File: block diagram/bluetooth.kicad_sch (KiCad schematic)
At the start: 0 parts

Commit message: add actual content
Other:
- removed sheet filtering
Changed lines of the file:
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@@
 	(wire
 		(pts
-			(xy 165.1 74.93) (xy 180.34 74.93)
+			(xy 165.1 74.93) (xy 205.74 74.93)
 		)
 		(stroke
@@
 		(pts
 			(xy 205.74 104.14) (xy 261.62 104.14)
-		)
-		(stroke
-			(width 0)
-			(type default)
-		)
-	)
-	(wire
-		(pts
-			(xy 195.58 74.93) (xy 205.74 74.93)
 		)
 		(stroke
@@
 				)
 			)
-		)
-	)
-	(sheet
-		(at 180.34 60.96)
-		(size 15.24 26.67)
-		(exclude_from_sim no)
-		(in_bom yes)
-		(on_board yes)
-		(dnp no)
-		(fields_autoplaced yes)
-		(stroke
-			(width 0.1524)
-			(type solid)
-			(color 132 0 0 1)
-		)
-		(fill
-			(color 255 255 194 1.0000)
-		)
-		(property "Sheetname" "filtering"
-			(at 180.34 60.2484 0)
-			(effects
-				(font
-					(size 1.27 1.27)
-				)
-				(justify left bottom)
-			)
-		)
-		(property "Sheetfile" "untitled.kicad_sch"
-			(at 180.34 88.2146 0)
-			(effects
-				(font
-					(size 1.27 1.27)
-				)
-				(justify left top)
-			)
-		)
-		(instances
-			(project "block diagram"
-				(path "/77b537aa-abd1-4b45-8666-f13206102f09/06c90ba9-5280-426d-b704-62779bf0bf86"
-					(page "11")
-				)
-			)

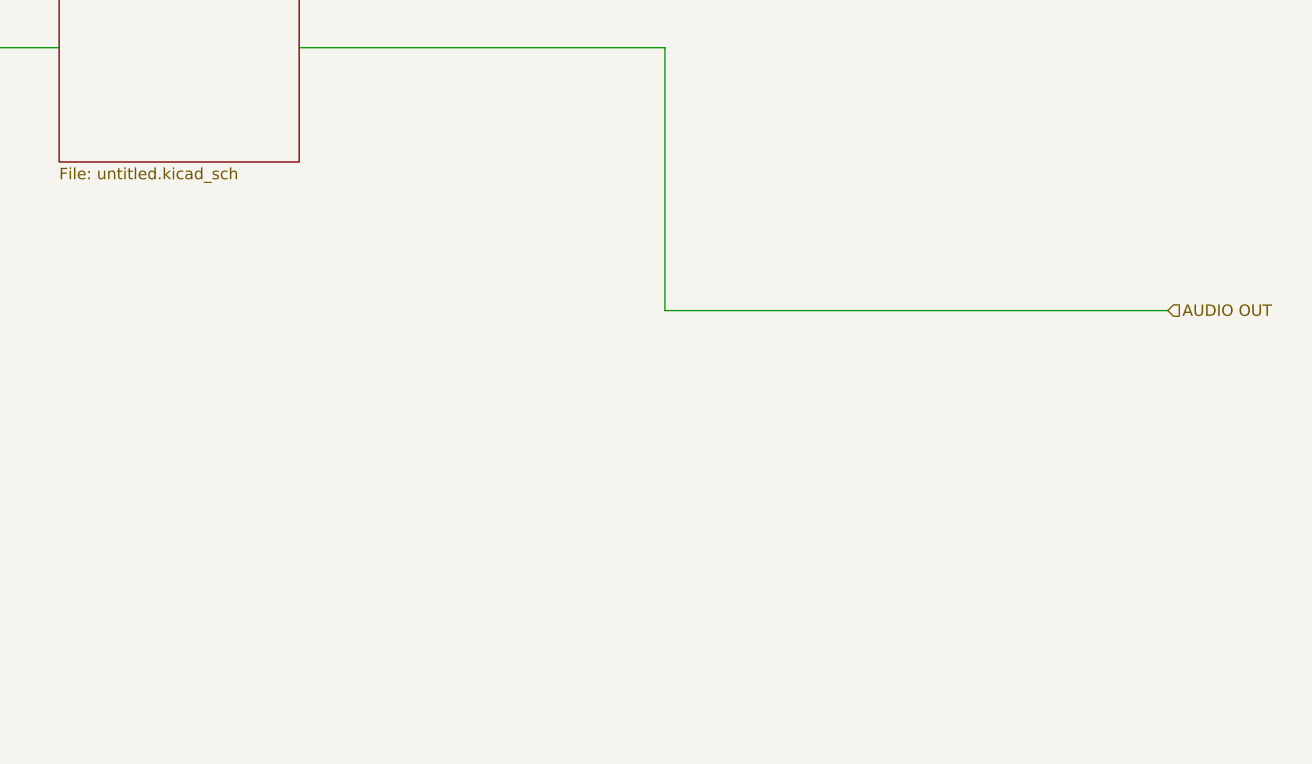
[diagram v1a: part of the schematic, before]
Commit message: battery spec added
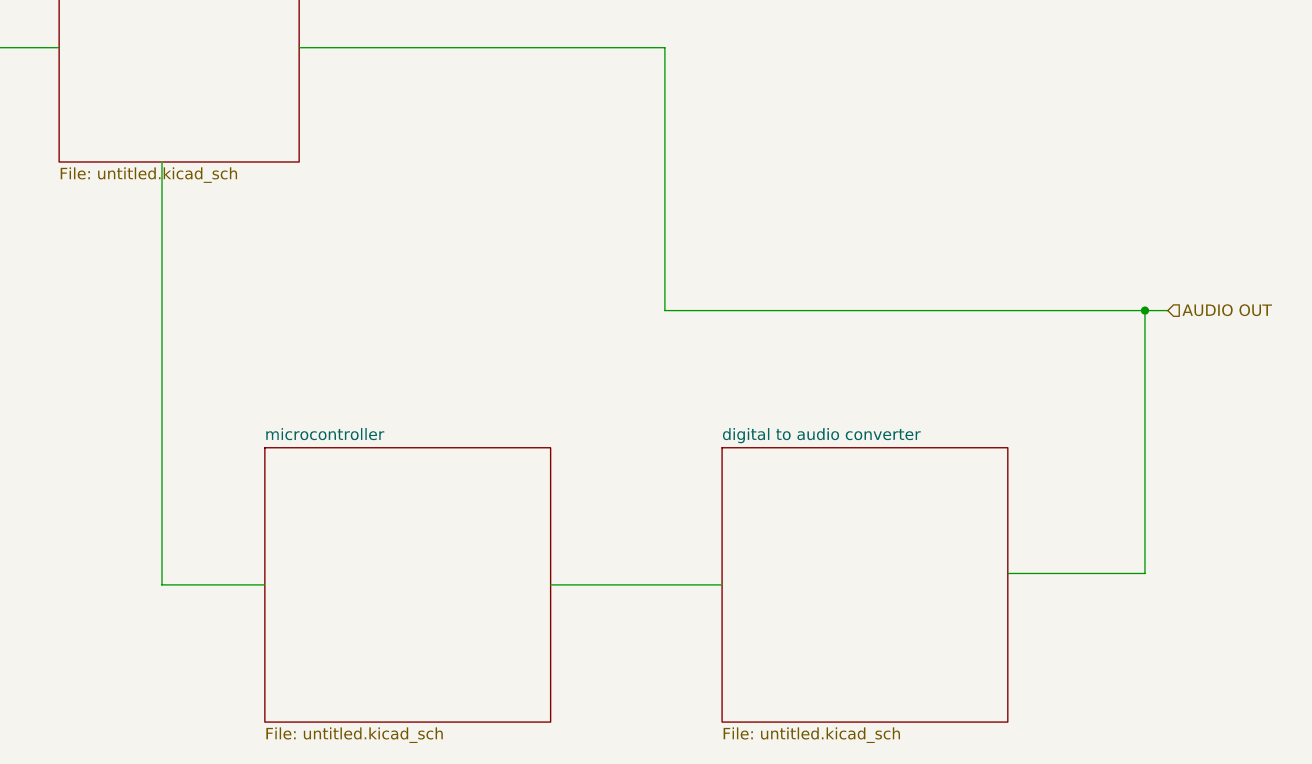
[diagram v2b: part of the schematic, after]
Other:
- added sheet digital to audio converter (untitled.kicad_sch)
- added sheet microcontroller (untitled.kicad_sch)
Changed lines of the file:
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@@
 	(generator_version "9.0")
 	(paper "A4")
+	(junction
+		(at 259.08 104.14)
+		(diameter 0)
+		(color 0 0 0 0)
+	)
 	(wire
 		(pts
@@
 	(wire
 		(pts
+			(xy 243.84 133.35) (xy 259.08 133.35)
+		)
+		(stroke
+			(width 0)
+			(type default)
+		)
+	)
+	(wire
+		(pts
 			(xy 116.84 35.56) (xy 116.84 62.23)
 		)
@@
 	(wire
 		(pts
+			(xy 149.86 87.63) (xy 149.86 134.62)
+		)
+		(stroke
+			(width 0)
+			(type default)
+		)
+	)
+	(wire
+		(pts
+			(xy 193.04 134.62) (xy 212.09 134.62)
+		)
+		(stroke
+			(width 0)
+			(type default)
+		)
+	)
+	(wire
+		(pts
 			(xy 139.7 31.75) (xy 53.34 31.75)
 		)
@@
 	(wire
 		(pts
-			(xy 205.74 104.14) (xy 261.62 104.14)
+			(xy 259.08 133.35) (xy 259.08 104.14)
+		)
+		(stroke
+			(width 0)
+			(type default)
+		)
+	)
+	(wire
+		(pts
+			(xy 205.74 104.14) (xy 259.08 104.14)
 		)
 		(stroke
@@
 	(wire
 		(pts
+			(xy 149.86 134.62) (xy 161.29 134.62)
+		)
+		(stroke
+			(width 0)
+			(type default)
+		)
+	)
+	(wire
+		(pts
 			(xy 60.96 74.93) (xy 71.12 74.93)
+		)
+		(stroke
+			(width 0)
+			(type default)
+		)
+	)
+	(wire
+		(pts
+			(xy 259.08 104.14) (xy 261.62 104.14)
 		)
 		(stroke
@@
 				)
 			)
+		)
+	)
+	(sheet
+		(at 161.29 119.38)
+		(size 31.75 30.48)
+		(exclude_from_sim no)
+		(in_bom yes)
+		(on_board yes)
+		(dnp no)
+		(fields_autoplaced yes)
+		(stroke
+			(width 0.1524)
+			(type solid)
+			(color 132 0 0 1)
+		)
+		(fill
+			(color 255 255 194 1.0000)
+		)
+		(property "Sheetname" "microcontroller"
+			(at 161.29 118.6684 0)
+			(effects
+				(font
+					(size 1.27 1.27)
+				)
+				(justify left bottom)
+			)
+		)
+		(property "Sheetfile" "untitled.kicad_sch"
+			(at 161.29 150.4446 0)
+			(effects
+				(font
+					(size 1.27 1.27)
+				)
+				(justify left top)
+			)
+		)
+		(instances
+			(project "block diagram"
+				(path "/77b537aa-abd1-4b45-8666-f13206102f09/06c90ba9-5280-426d-b704-62779bf0bf86"
+					(page "11")
+				)
+			)
+		)
+	)
+	(sheet
+		(at 212.09 119.38)
+		(size 31.75 30.48)
+		(exclude_from_sim no)
+		(in_bom yes)
+		(on_board yes)
+		(dnp no)
+		(fields_autoplaced yes)
+		(stroke
+			(width 0.1524)
+			(type solid)
+			(color 132 0 0 1)
+		)
+		(fill
+			(color 255 255 194 1.0000)
+		)
+		(property "Sheetname" "digital to audio converter"
+			(at 212.09 118.6684 0)
+			(effects
+				(font
+					(size 1.27 1.27)
+				)
+				(justify left bottom)
+			)
+		)
+		(property "Sheetfile" "untitled.kicad_sch"
+			(at 212.09 150.4446 0)
+			(effects
+				(font
+					(size 1.27 1.27)
+				)
+				(justify left top)
+			)
+		)
+		(instances
+			(project "block diagram"
+				(path "/77b537aa-abd1-4b45-8666-f13206102f09/06c90ba9-5280-426d-b704-62779bf0bf86"
+					(page "12")
+				)
+			)

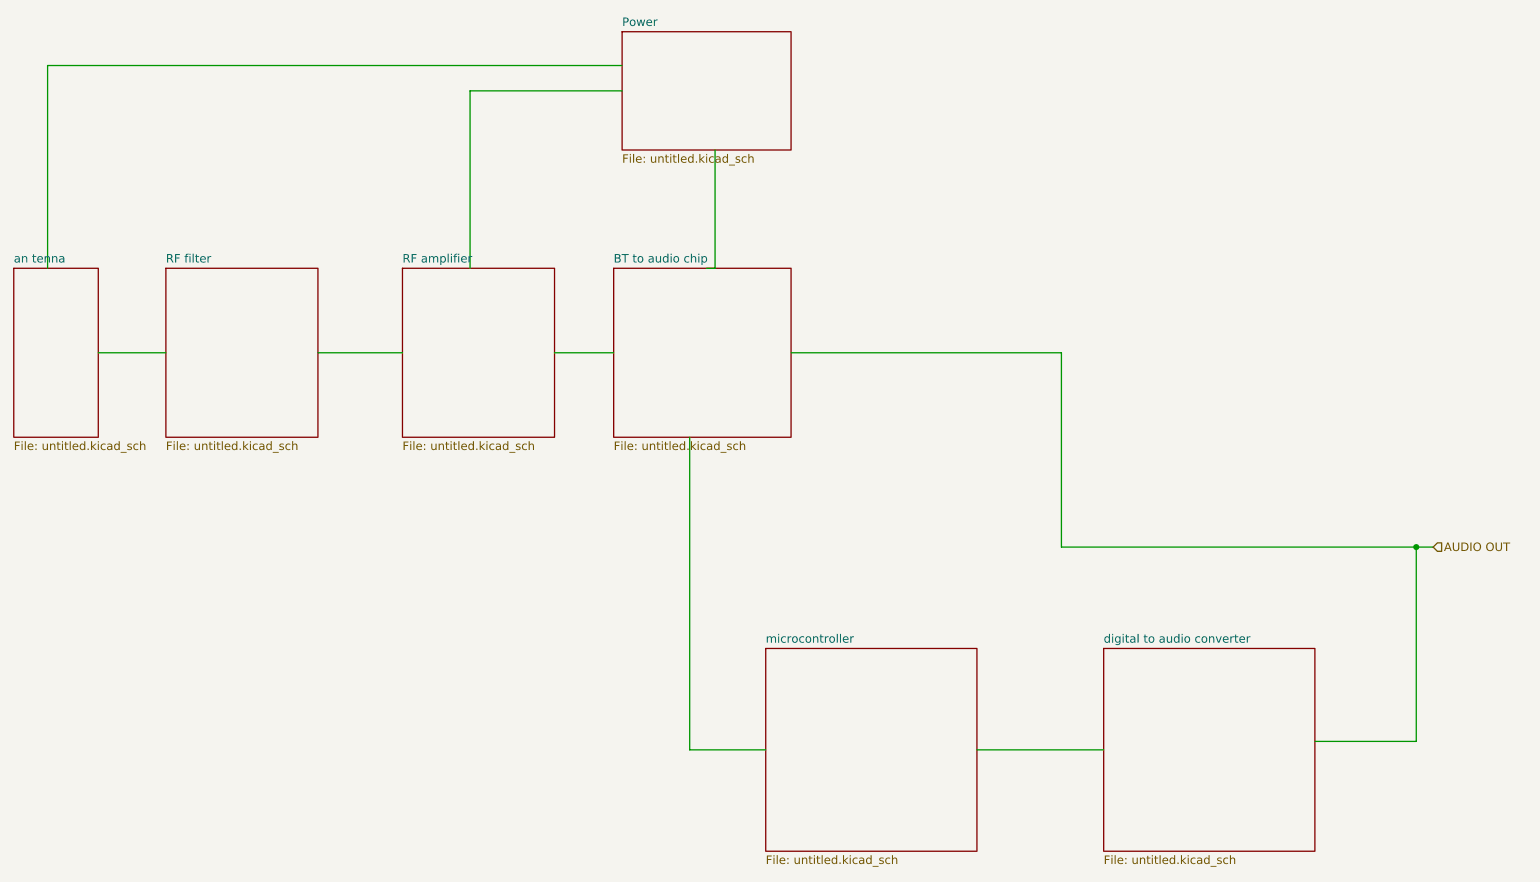
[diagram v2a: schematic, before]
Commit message: diagrammed bt chip, please fix formatting
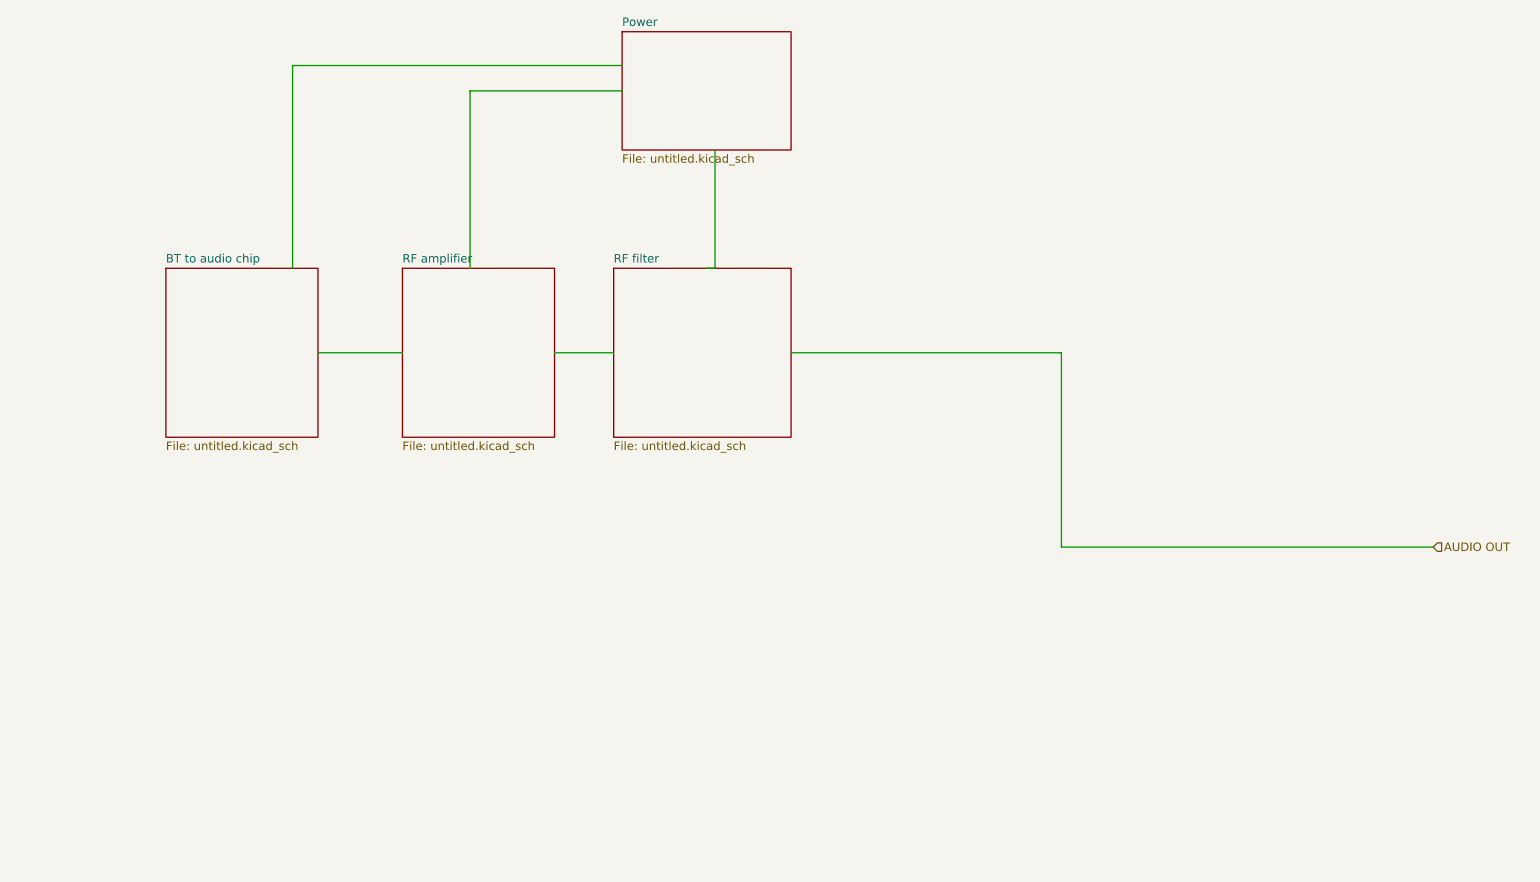
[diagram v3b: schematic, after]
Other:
- removed sheet an tenna
- removed sheet digital to audio converter
- removed sheet microcontroller
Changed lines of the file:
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@@
 (kicad_sch
-	(version 20250114)
+	(version 20260306)
 	(generator "eeschema")
-	(generator_version "9.0")
+	(generator_version "10.0")
 	(paper "A4")
-	(junction
-		(at 259.08 104.14)
-		(diameter 0)
-		(color 0 0 0 0)
-	)
-	(wire
-		(pts
-			(xy 53.34 31.75) (xy 53.34 62.23)
+	(wire
+		(pts
+			(xy 90.17 31.75) (xy 90.17 62.23)
 		)
 		(stroke
@@
 	(wire
 		(pts
-			(xy 243.84 133.35) (xy 259.08 133.35)
-		)
-		(stroke
-			(width 0)
-			(type default)
-		)
-	)
-	(wire
-		(pts
 			(xy 116.84 35.56) (xy 116.84 62.23)
 		)
@@
 	(wire
 		(pts
-			(xy 149.86 87.63) (xy 149.86 134.62)
-		)
-		(stroke
-			(width 0)
-			(type default)
-		)
-	)
-	(wire
-		(pts
-			(xy 193.04 134.62) (xy 212.09 134.62)
-		)
-		(stroke
-			(width 0)
-			(type default)
-		)
-	)
-	(wire
-		(pts
-			(xy 139.7 31.75) (xy 53.34 31.75)
-		)
-		(stroke
-			(width 0)
-			(type default)
-		)
-	)
-	(wire
-		(pts
 			(xy 205.74 74.93) (xy 205.74 104.14)
 		)
@@
 	(wire
 		(pts
-			(xy 259.08 133.35) (xy 259.08 104.14)
-		)
-		(stroke
-			(width 0)
-			(type default)
-		)
-	)
-	(wire
-		(pts
-			(xy 205.74 104.14) (xy 259.08 104.14)
+			(xy 205.74 104.14) (xy 261.62 104.14)
+		)
+		(stroke
+			(width 0)
+			(type default)
+		)
+	)
+	(wire
+		(pts
+			(xy 139.7 31.75) (xy 90.17 31.75)
 		)
 		(stroke
@@
 		(pts
 			(xy 93.98 74.93) (xy 106.68 74.93)
-		)
-		(stroke
-			(width 0)
-			(type default)
-		)
-	)
-	(wire
-		(pts
-			(xy 149.86 134.62) (xy 161.29 134.62)
-		)
-		(stroke
-			(width 0)
-			(type default)
-		)
-	)
-	(wire
-		(pts
-			(xy 60.96 74.93) (xy 71.12 74.93)
-		)
-		(stroke
-			(width 0)
-			(type default)
-		)
-	)
-	(wire
-		(pts
-			(xy 259.08 104.14) (xy 261.62 104.14)
 		)
 		(stroke
@@
 		)
 		(fill
-			(color 255 255 194 1.0000)
+			(color 255 255 194 1)
 		)
 		(property "Sheetname" "RF amplifier"
 			(at 106.68 61.5184 0)
+			(show_name no)
+			(do_not_autoplace no)
 			(effects
 				(font
@@
 		(property "Sheetfile" "untitled.kicad_sch"
 			(at 106.68 88.2146 0)
+			(show_name no)
+			(do_not_autoplace no)
 			(effects
 				(font
@@
 	)
 	(sheet
-		(at 161.29 119.38)
-		(size 31.75 30.48)
-		(exclude_from_sim no)
-		(in_bom yes)
-		(on_board yes)
-		(dnp no)
-		(fields_autoplaced yes)
-		(stroke
-			(width 0.1524)
-			(type solid)
-			(color 132 0 0 1)
-		)
-		(fill
-			(color 255 255 194 1.0000)
-		)
-		(property "Sheetname" "microcontroller"
-			(at 161.29 118.6684 0)
-			(effects
-				(font
-					(size 1.27 1.27)
-				)
-				(justify left bottom)
-			)
-		)
-		(property "Sheetfile" "untitled.kicad_sch"
-			(at 161.29 150.4446 0)
-			(effects
-				(font
-					(size 1.27 1.27)
-				)
-				(justify left top)
-			)
-		)
-		(instances
-			(project "block diagram"
-				(path "/77b537aa-abd1-4b45-8666-f13206102f09/06c90ba9-5280-426d-b704-62779bf0bf86"
-					(page "11")
-				)
-			)
-		)
-	)
-	(sheet
-		(at 212.09 119.38)
-		(size 31.75 30.48)
-		(exclude_from_sim no)
-		(in_bom yes)
-		(on_board yes)
-		(dnp no)
-		(fields_autoplaced yes)
-		(stroke
-			(width 0.1524)
-			(type solid)
-			(color 132 0 0 1)
-		)
-		(fill
-			(color 255 255 194 1.0000)
-		)
-		(property "Sheetname" "digital to audio converter"
-			(at 212.09 118.6684 0)
-			(effects
-				(font
-					(size 1.27 1.27)
-				)
-				(justify left bottom)
-			)
-		)
-		(property "Sheetfile" "untitled.kicad_sch"
-			(at 212.09 150.4446 0)
-			(effects
-				(font
-					(size 1.27 1.27)
-				)
-				(justify left top)
-			)
-		)
-		(instances
-			(project "block diagram"
-				(path "/77b537aa-abd1-4b45-8666-f13206102f09/06c90ba9-5280-426d-b704-62779bf0bf86"
-					(page "12")
-				)
-			)
-		)
-	)
-	(sheet
 		(at 139.7 26.67)
 		(size 25.4 17.78)
@@
 		)
 		(fill
-			(color 255 255 194 1.0000)
+			(color 255 255 194 1)
 		)
 		(property "Sheetname" "Power"
 			(at 139.7 25.9584 0)
+			(show_name no)
+			(do_not_autoplace no)
 			(effects
 				(font
@@
 		(property "Sheetfile" "untitled.kicad_sch"
 			(at 139.7 45.0346 0)
+			(show_name no)
+			(do_not_autoplace no)
 			(effects
 				(font
@@
 		(property "Field2" ""
 			(at 139.7 26.67 0)
+			(show_name no)
+			(do_not_autoplace no)
 			(effects
 				(font
@@
 		)
 		(fill
-			(color 255 255 194 1.0000)
-		)
-		(property "Sheetname" "BT to audio chip"
+			(color 255 255 194 1)
+		)
+		(property "Sheetname" "RF filter"
 			(at 138.43 61.5184 0)
+			(show_name no)
+			(do_not_autoplace no)
 			(effects
 				(font
@@
 		(property "Sheetfile" "untitled.kicad_sch"
 			(at 138.43 88.2146 0)
+			(show_name no)
+			(do_not_autoplace no)
 			(effects
 				(font
@@
 	)
 	(sheet
-		(at 48.26 62.23)
-		(size 12.7 25.4)
-		(exclude_from_sim no)
-		(in_bom yes)
-		(on_board yes)
-		(dnp no)
-		(fields_autoplaced yes)
-		(stroke
-			(width 0.1524)
-			(type solid)
-			(color 132 0 0 1)
-		)
-		(fill
-			(color 255 255 194 1.0000)
-		)
-		(property "Sheetname" "an tenna"
-			(at 48.26 61.5184 0)
-			(effects
-				(font
-					(size 1.27 1.27)
-				)
-				(justify left bottom)
-			)
-		)
-		(property "Sheetfile" "untitled.kicad_sch"
-			(at 48.26 88.2146 0)
-			(effects
-				(font
-					(size 1.27 1.27)
-				)
-				(justify left top)
-			)
-		)
-		(instances
-			(project "block diagram"
-				(path "/77b537aa-abd1-4b45-8666-f13206102f09/06c90ba9-5280-426d-b704-62779bf0bf86"
-					(page "7")
-				)
-			)
-		)
-	)
-	(sheet
 		(at 71.12 62.23)
 		(size 22.86 25.4)
@@
 		)
 		(fill
-			(color 255 255 194 1.0000)
-		)
-		(property "Sheetname" "RF filter"
+			(color 255 255 194 1)
+		)
+		(property "Sheetname" "BT to audio chip"
 			(at 71.12 61.5184 0)
+			(show_name no)
+			(do_not_autoplace no)
 			(effects
 				(font
@@
 		(property "Sheetfile" "untitled.kicad_sch"
 			(at 71.12 88.2146 0)
-			(effects
-				(font
+			(show_name no)
+			(do_not_autoplace no)
+			(effects
+				(font
